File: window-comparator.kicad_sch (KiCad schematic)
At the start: 10 parts, among them U22001 TLV9352

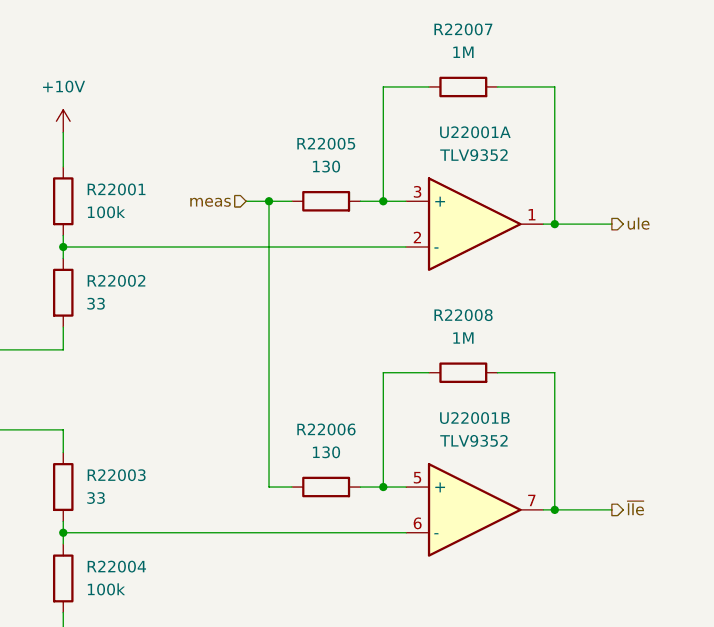
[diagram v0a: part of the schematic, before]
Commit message: edit window-comparator feedback prof spiegelberg, remove hysteresis at window comparator
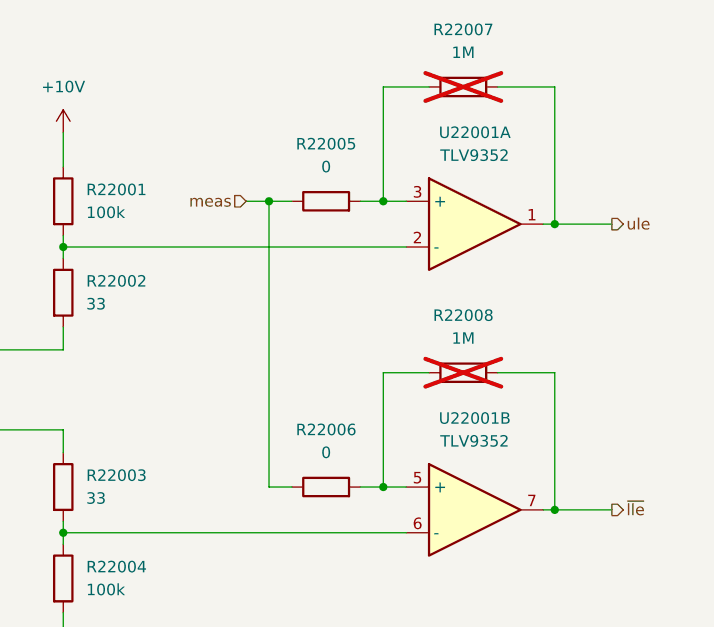
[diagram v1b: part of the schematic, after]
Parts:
- R22005, R22006: value 130 -> 0; MPN RC1210FR-07130RL -> RC1210JR-070RL; VPN 603-RC1210FR-07130RL -> 603-RC1210JR-070RL
- R22007, R22008: now not fitted; now left out of the parts list
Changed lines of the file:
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@@
 		(unit 1)
 		(exclude_from_sim no)
-		(in_bom yes)
-		(on_board yes)
-		(dnp no)
+		(in_bom no)
+		(on_board yes)
+		(dnp yes)
 		(fields_autoplaced yes)
 		(property "Reference" "R22007"
@@
 			)
 		)
-		(property "Value" "130"
+		(property "Value" "0"
 			(at 146.05 105.41 90)
 			(effects
@@
 			)
 		)
-		(property "MPN" "RC1210FR-07130RL"
+		(property "MPN" "RC1210JR-070RL"
 			(at 146.05 109.22 0)
 			(effects
@@
 			)
 		)
-		(property "VPN" "603-RC1210FR-07130RL"
+		(property "VPN" "603-RC1210JR-070RL"
 			(at 146.05 109.22 0)
 			(effects
@@
 		(unit 1)
 		(exclude_from_sim no)
-		(in_bom yes)
-		(on_board yes)
-		(dnp no)
+		(in_bom no)
+		(on_board yes)
+		(dnp yes)
 		(fields_autoplaced yes)
 		(property "Reference" "R22008"
@@
 			)
 		)
-		(property "Value" "130"
+		(property "Value" "0"
 			(at 146.05 73.66 90)
 			(effects
@@
 			)
 		)
-		(property "MPN" "RC1210FR-07130RL"
+		(property "MPN" "RC1210JR-070RL"
 			(at 146.05 77.47 0)
 			(effects
@@
 			)
 		)
-		(property "VPN" "603-RC1210FR-07130RL"
+		(property "VPN" "603-RC1210JR-070RL"
 			(at 146.05 77.47 0)
 			(effects

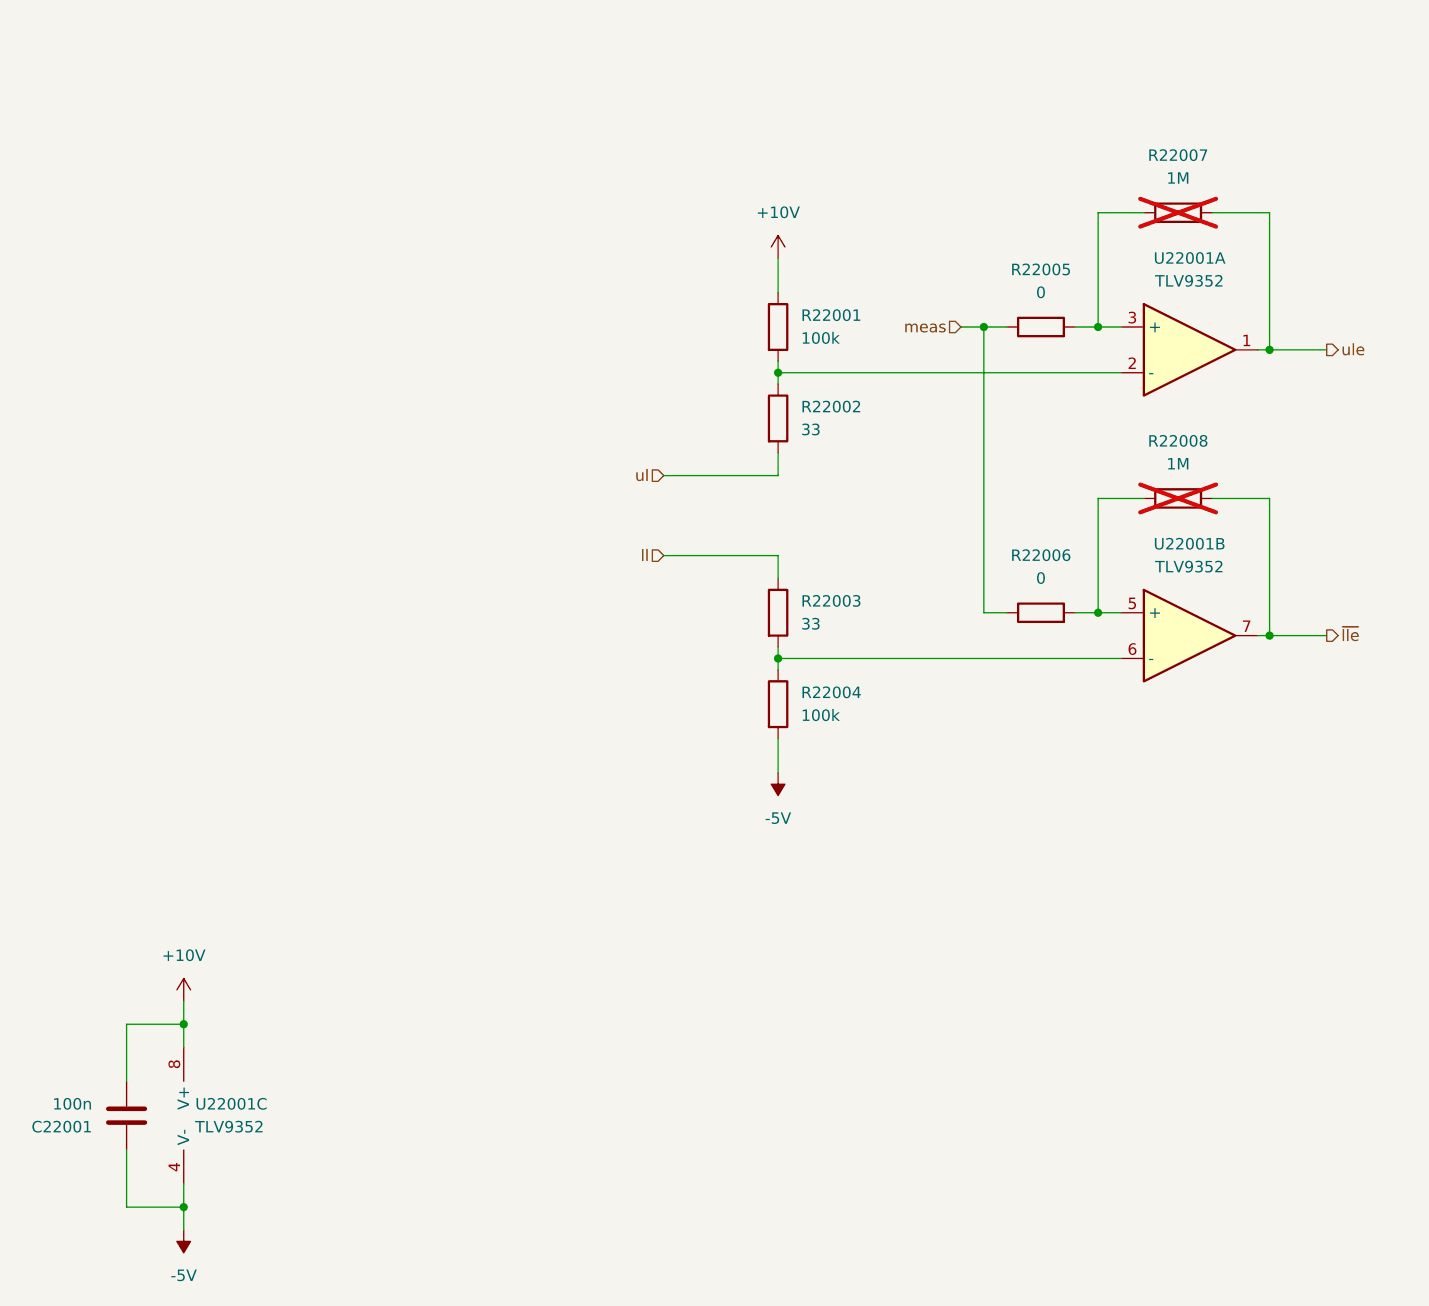
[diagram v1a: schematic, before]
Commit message: edit window-comparator feedback prof spiegelberg, add trimmer to window generation
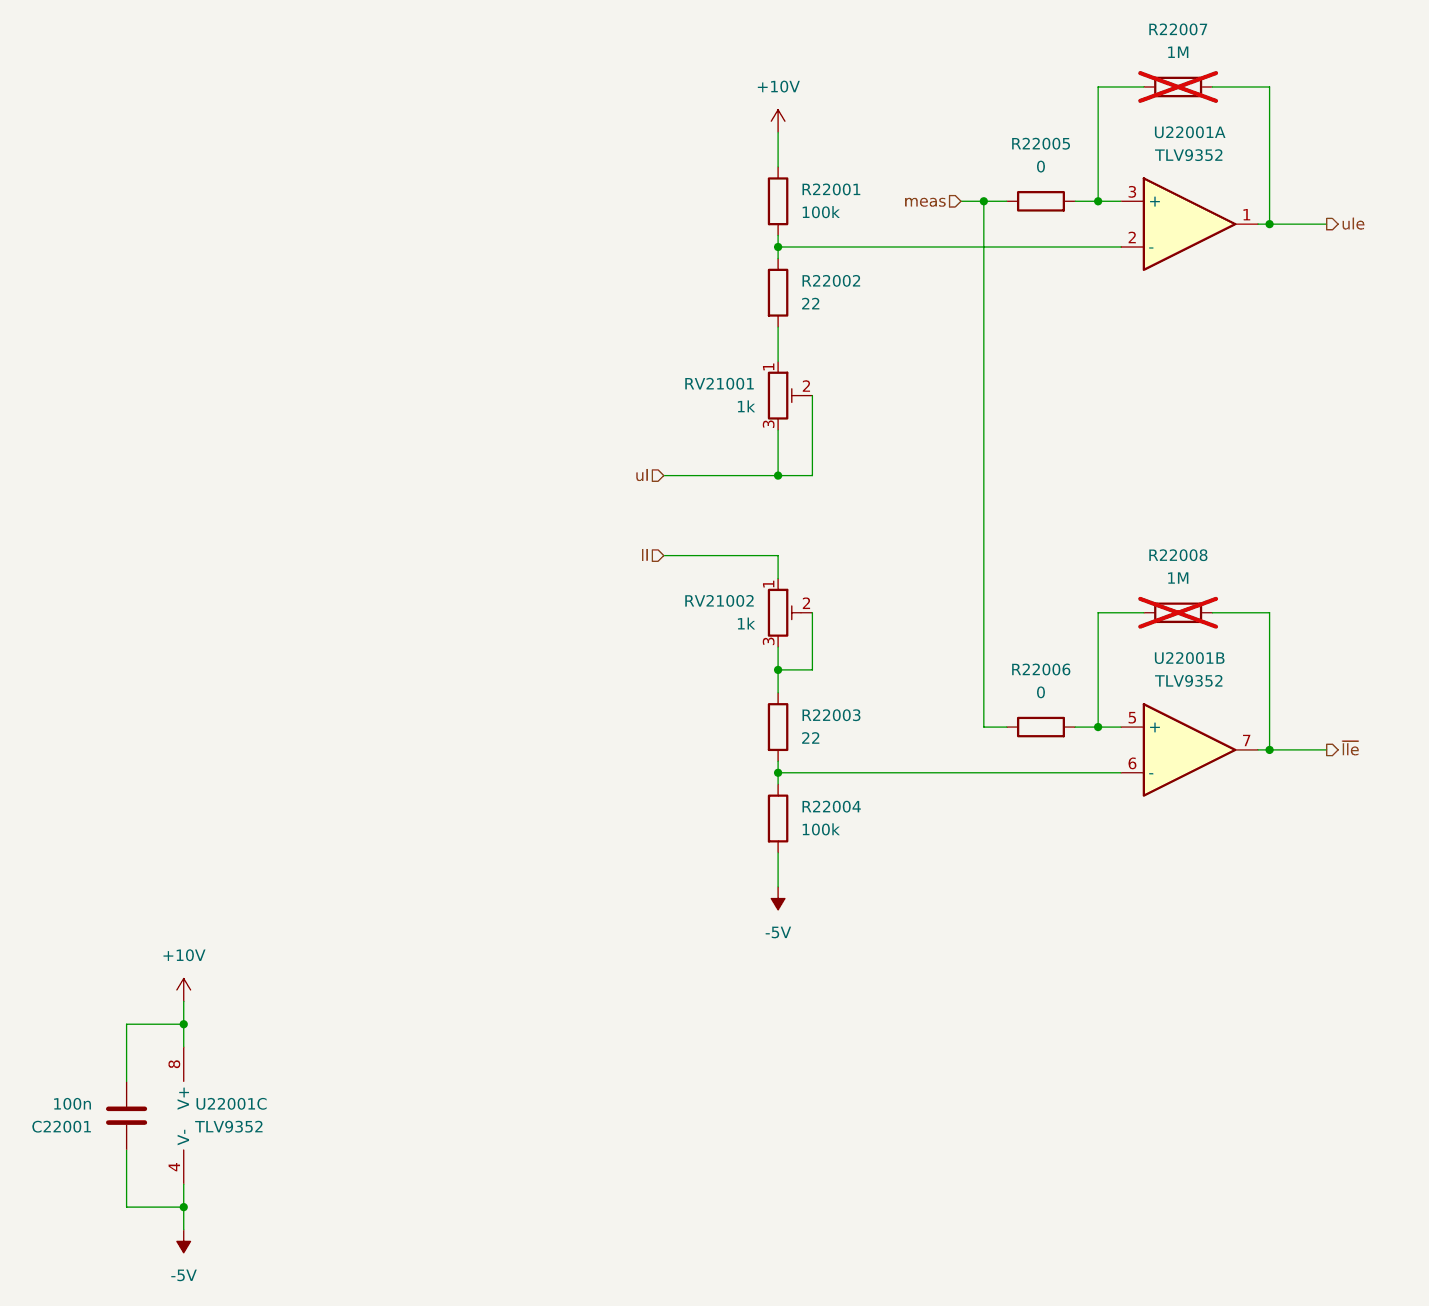
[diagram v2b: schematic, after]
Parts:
- added RV21001, RV21002: 1k, pss:Potentiometer_Bourns_PVG5A, symbol Device:R_Potentiometer_Trim
- R22002, R22003: value 33 -> 22; MPN RC1210FR-0733RL -> RC1210FR-0722RL; VPN 603-RC1210FR-0733RL -> 603-RC1210FR-0722RL
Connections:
- net ll: now also RV21002.1; no longer R22003.1
- net ul: now also RV21001.2, RV21001.3; no longer R22002.2
- new net: R22002.2, RV21001.1
- new net: R22003.1, RV21002.2, RV21002.3
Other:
- moved on the sheet: R22001, R22002, R22003, R22004, R22005, R22006, R22007, R22008, U22001A, U22001B

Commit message: edit trimmers use adjustmentstyle 'top' for trimmers
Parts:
- RV21001, RV21002: MPN PVG5H102C03B00 -> PVG5A102C03B00; VPN 81-PVG5H102C03B00 -> 81-PVG5A102C03B00
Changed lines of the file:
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@@
 			)
 		)
-		(property "MPN" "PVG5H102C03B00"
+		(property "MPN" "PVG5A102C03B00"
 			(at 116.84 109.22 0)
 			(effects
@@
 			)
 		)
-		(property "VPN" "81-PVG5H102C03B00"
+		(property "VPN" "81-PVG5A102C03B00"
 			(at 116.84 109.22 0)
 			(effects
@@
 			)
 		)
-		(property "MPN" "PVG5H102C03B00"
+		(property "MPN" "PVG5A102C03B00"
 			(at 116.84 85.09 0)
 			(effects
@@
 			)
 		)
-		(property "VPN" "81-PVG5H102C03B00"
+		(property "VPN" "81-PVG5A102C03B00"
 			(at 116.84 85.09 0)
 			(effects
